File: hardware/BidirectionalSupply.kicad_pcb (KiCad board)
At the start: 4 copper layers, 132 x 107 mm, 182 parts, among them J1 USB-309GC-B-SU, J10 Conn_01x02, J11 Conn_01x08, J12 Conn_01x05, J13 Conn_01x02, J2 CON10, J3 CON2, J6 CON4, J7 CON2, J8 Conn_01x03, J9 Conn_01x12, Q1 SIR880BDP, Q10 SIR880BDP, Q11 SIR880BDP, Q12 SIR880BDP, Q2 SIR880BDP, Q3 SIR880BDP, Q4 SIR880BDP, Q5 SIR880BDP, Q6 SIR880BDP, Q7 SIR880BDP, Q8 SIR880BDP, Q9 SIR880BDP, SW1 SW_Push, SW2 SW_Push, U1 W25Q128JVS, U2 LM74810QDRRRQ1, U3 RP2350_60QFN, U4 BQ25758, U5 MAX17502EATB+T, U6 LM74810QDRRRQ1, U7 LM74810QDRRRQ1, U8 LM74810QDRRRQ1, Y1 ABM8-272-T3

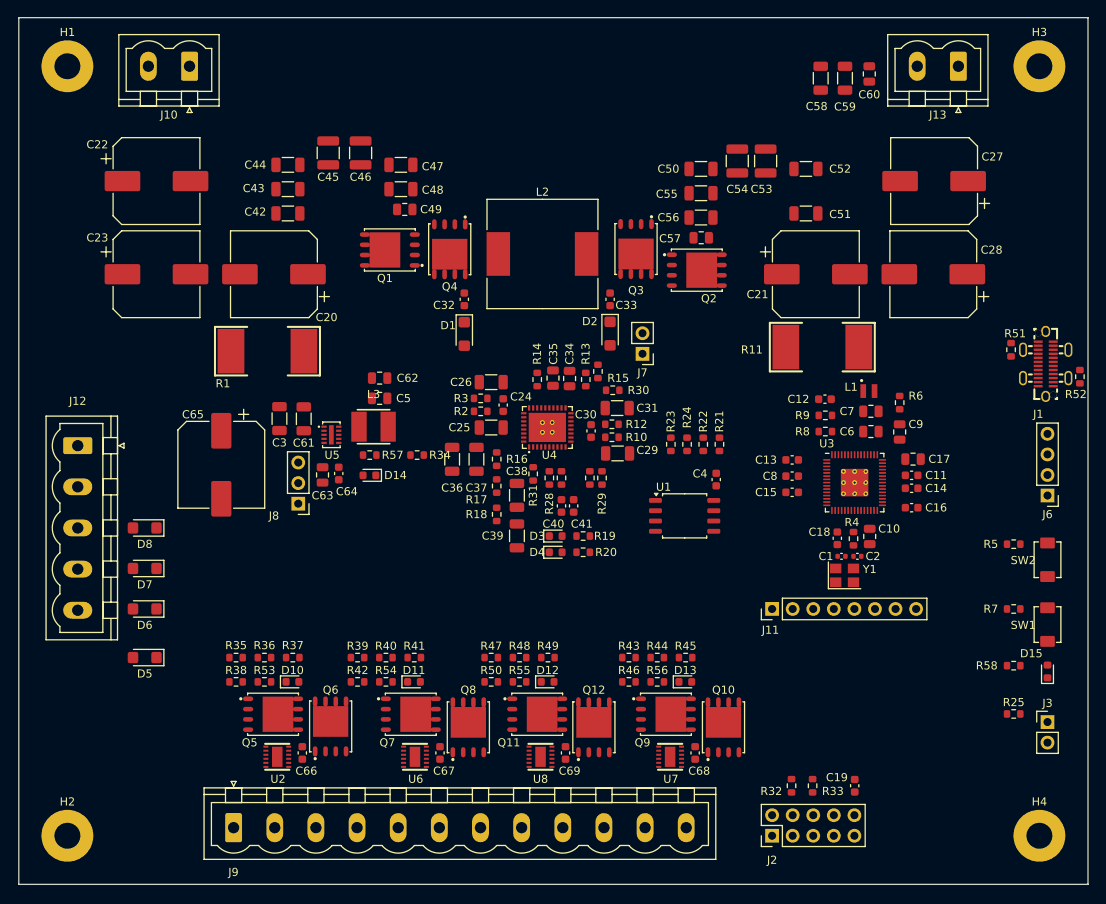
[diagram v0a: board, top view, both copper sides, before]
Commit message: - Routed board with all fixable DRC errors and warnings fixed
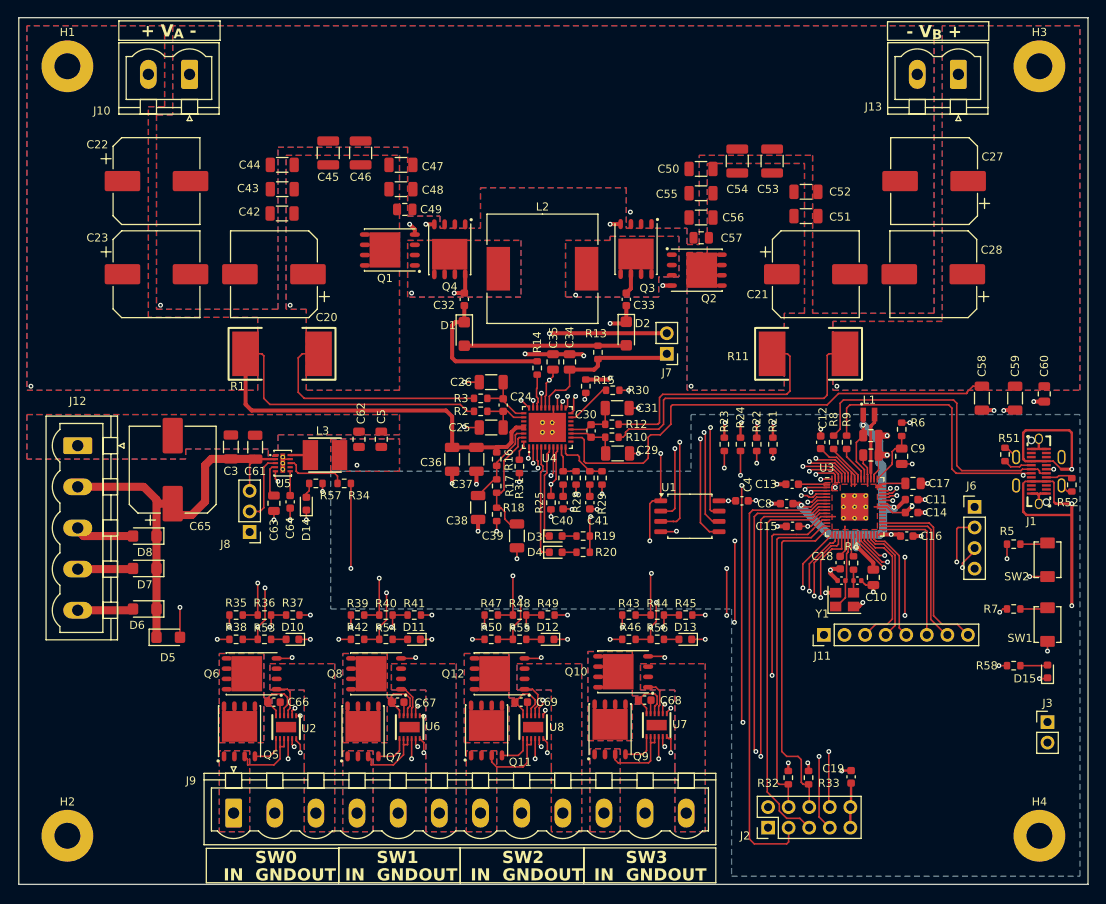
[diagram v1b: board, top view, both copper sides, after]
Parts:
- C1, C2: footprint Capacitor_SMD:C_0402_1005Metric -> BidirectionalSupply:C_0402_DRC
- Y1: footprint Crystal:Crystal_SMD_3225-4Pin_3.2x2.5mm -> BidirectionalSupply:Crystal_SMD_3225-4Pin_DRC
- moved R25 62.8 mm to (115.7, 109.9), turned to 90 degrees
- moved C60 45.0 mm to (176.6, 96.5)
- moved C59 44.7 mm to (173.0, 97.0)
- moved C58 44.2 mm to (168.9, 97.0)
- moved Q10 14.2 mm to (124.6, 130.8), turned to 90 degrees
- moved R52 13.4 mm to (180.0, 107.7)
- moved Q12 13.4 mm to (109.4, 131.0), turned to 90 degrees
- moved J1 13.3 mm to (175.9, 106.0)
- moved Q8 13.2 mm to (94.1, 131.0), turned to 90 degrees
- moved R51 12.9 mm to (171.8, 103.9)
- moved Q6 11.7 mm to (78.8, 131.0), turned to 90 degrees
- moved R34 9.66 mm to (90.2, 107.5)
- moved J6 9.11 mm to (168.0, 110.4), turned to 0 degrees
- moved C68 9.02 mm to (127.3, 134.2), turned to 0 degrees
- moved D14 8.54 mm to (85.5, 110.0), turned to 90 degrees
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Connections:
- C27 pad 1: Net-(J13-Pin_2) -> Net-(J13-Pin_1)
- C28 pad 1: Net-(J13-Pin_2) -> Net-(J13-Pin_1)
- C58 pad 1: Net-(J13-Pin_2) -> Net-(J13-Pin_1)
- C59 pad 1: Net-(J13-Pin_2) -> Net-(J13-Pin_1)
- C60 pad 1: Net-(J13-Pin_2) -> Net-(J13-Pin_1)
- J11 pad 1: Net-(J11-Pin_1) -> GND
- J11 pad 2: Net-(J11-Pin_2) -> +3V3
- J13 pad 1: GND -> Net-(J13-Pin_1)
- J13 pad 2: Net-(J13-Pin_2) -> GND
- J9 pad 1: GND -> Net-(J9-Pin_1)
- J9 pad 10: GND -> Net-(J9-Pin_10)
- J9 pad 11: Net-(J9-Pin_11) -> GND
- J9 pad 2: Net-(J9-Pin_2) -> GND
- J9 pad 4: GND -> Net-(J9-Pin_4)
- J9 pad 5: Net-(J9-Pin_5) -> GND
- J9 pad 7: GND -> Net-(J9-Pin_7)
- J9 pad 8: Net-(J9-Pin_8) -> GND
- Q11 pad 1: Net-(J9-Pin_8) -> Net-(J9-Pin_7)
- Q11 pad 2: Net-(J9-Pin_8) -> Net-(J9-Pin_7)
- Q11 pad 3: Net-(J9-Pin_8) -> Net-(J9-Pin_7)
- Q5 pad 1: Net-(J9-Pin_2) -> Net-(J9-Pin_1)
- Q5 pad 2: Net-(J9-Pin_2) -> Net-(J9-Pin_1)
- Q5 pad 3: Net-(J9-Pin_2) -> Net-(J9-Pin_1)
- Q7 pad 1: Net-(J9-Pin_5) -> Net-(J9-Pin_4)
- Q7 pad 2: Net-(J9-Pin_5) -> Net-(J9-Pin_4)
- Q7 pad 3: Net-(J9-Pin_5) -> Net-(J9-Pin_4)
- Q9 pad 1: Net-(J9-Pin_11) -> Net-(J9-Pin_10)
- Q9 pad 2: Net-(J9-Pin_11) -> Net-(J9-Pin_10)
- Q9 pad 3: Net-(J9-Pin_11) -> Net-(J9-Pin_10)
- R10 pad 1: Net-(J13-Pin_2) -> Net-(J13-Pin_1)
- R11 pad 1: Net-(J13-Pin_2) -> Net-(J13-Pin_1)
- U2 pad 2: Net-(J9-Pin_2) -> Net-(J9-Pin_1)
- U2 pad 3: Net-(J9-Pin_2) -> Net-(J9-Pin_1)
- U3 pad 16: Net-(J11-Pin_1) -> SW0_EN
- U3 pad 17: Net-(J11-Pin_2) -> SW1_EN
- U3 pad 18: Net-(J11-Pin_3) -> SW2_EN
- U3 pad 19: Net-(J11-Pin_4) -> SW3_EN
- U3 pad 27: Net-(J11-Pin_5) -> Net-(J11-Pin_3)
- U3 pad 28: Net-(J11-Pin_6) -> Net-(J11-Pin_4)
- U3 pad 29: Net-(J11-Pin_7) -> Net-(J11-Pin_5)
- U3 pad 31: Net-(J11-Pin_8) -> Net-(J11-Pin_6)
- U3 pad 32: unconnected-(U3-GPIO20-Pad32) -> Net-(J11-Pin_7)
- U3 pad 33: unconnected-(U3-GPIO21-Pad33) -> Net-(J11-Pin_8)
- U3 pad 34: SW0_EN -> unconnected-(U3-GPIO22-Pad34)
- U3 pad 35: SW1_EN -> unconnected-(U3-GPIO23-Pad35)
- U3 pad 36: SW2_EN -> unconnected-(U3-GPIO24-Pad36)
- U3 pad 37: SW3_EN -> unconnected-(U3-GPIO25-Pad37)
- U3 pad 4: ~{BQ_CE} -> ~{BQ_INT}
- U3 pad 5: ~{BQ_INT} -> ~{BQ_CE}
- U4 pad 12: Net-(J13-Pin_2) -> Net-(J13-Pin_1)
- U6 pad 2: Net-(J9-Pin_5) -> Net-(J9-Pin_4)
- U6 pad 3: Net-(J9-Pin_5) -> Net-(J9-Pin_4)
- U7 pad 2: Net-(J9-Pin_11) -> Net-(J9-Pin_10)
- U7 pad 3: Net-(J9-Pin_11) -> Net-(J9-Pin_10)
- U8 pad 2: Net-(J9-Pin_8) -> Net-(J9-Pin_7)
- U8 pad 3: Net-(J9-Pin_8) -> Net-(J9-Pin_7)
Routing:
- net Net-(D5-A): track 0.00 -> 169.6 mm, vias 0 -> 4
- net Net-(U3-RUN): track 0.00 -> 113.0 mm, vias 0 -> 7
- net SW0_EN: track 0.00 -> 105.4 mm, vias 0 -> 4
- net GND: track 0.00 -> 102.1 mm, vias 0 -> 61
- net Net-(J13-Pin_1): track 0.00 -> 97.5 mm, vias 0 -> 1
- net Net-(J3-Pin_1): track 0.00 -> 96.9 mm, vias 0 -> 3
- net SW0_VSENSE: track 0.00 -> 94.4 mm, vias 0 -> 2
- net SW1_EN: track 0.00 -> 91.6 mm, vias 0 -> 4
- net /Microcontroller/QSPI_SS: track 0.00 -> 90.9 mm, vias 0 -> 6
- net CNV_VIN: track 0.00 -> 82.5 mm, vias 0 -> 1
- net SW1_VSENSE: track 0.00 -> 81.4 mm, vias 0 -> 2
- net SW2_EN: track 0.00 -> 74.5 mm, vias 0 -> 4
- net +3V3: track 0.00 -> 72.8 mm, vias 0 -> 16
- net SW2_VSENSE: track 0.00 -> 65.7 mm, vias 0 -> 2
- net LED: track 0.00 -> 59.0 mm, vias 0 -> 2
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- added copper zone on B.Cu, net +3V3
- added copper zone on F.Cu, net +3V3
- added copper zone on B.Cu, net CNV_VIN
- added copper zone on F.Cu, net CNV_VIN
- added copper zone on B.Cu, net GND
- added copper zone on F.Cu, net GND
- added copper zone on In1.Cu, net GND
- added copper zone on B.Cu, net Net-(J13-Pin_1)
- added copper zone on F.Cu, net Net-(J13-Pin_1)
- added copper zone on B.Cu, net Net-(J9-Pin_1)
- added copper zone on F.Cu, net Net-(J9-Pin_1)
- added copper zone on B.Cu, net Net-(J9-Pin_10)
- added copper zone on F.Cu, net Net-(J9-Pin_10)
- added copper zone on B.Cu, net Net-(J9-Pin_12)
- added copper zone on F.Cu, net Net-(J9-Pin_12)
- added copper zone on B.Cu, net Net-(J9-Pin_3)
- added copper zone on F.Cu, net Net-(J9-Pin_3)
- added copper zone on B.Cu, net Net-(J9-Pin_4)
- added copper zone on F.Cu, net Net-(J9-Pin_4)
- added copper zone on B.Cu, net Net-(J9-Pin_6)
- added copper zone on F.Cu, net Net-(J9-Pin_6)
- added copper zone on B.Cu, net Net-(J9-Pin_7)
- added copper zone on F.Cu, net Net-(J9-Pin_7)
- added copper zone on B.Cu, net Net-(J9-Pin_9)
- added copper zone on F.Cu, net Net-(J9-Pin_9)
- added copper zone on B.Cu, net Net-(Q1-EP)
- added copper zone on F.Cu, net Net-(Q1-EP)
- added copper zone on B.Cu, net Net-(Q10-EP)
- added copper zone on F.Cu, net Net-(Q10-EP)
- added copper zone on B.Cu, net Net-(Q11-EP)
- added copper zone on F.Cu, net Net-(Q11-EP)
- added copper zone on B.Cu, net Net-(Q2-EP)
- added copper zone on F.Cu, net Net-(Q2-EP)
- added copper zone on B.Cu, net Net-(Q3-EP)
- added copper zone on F.Cu, net Net-(Q3-EP)
- added copper zone on B.Cu, net Net-(Q4-EP)
- added copper zone on F.Cu, net Net-(Q4-EP)
- added copper zone on B.Cu, net Net-(Q5-EP)
- added copper zone on F.Cu, net Net-(Q5-EP)
- added copper zone on B.Cu, net Net-(Q7-EP)
- added copper zone on F.Cu, net Net-(Q7-EP)
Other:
- board text added: "+ V_{A} -"
- board text added: "- V_{B} +"
- board text added: "GND"
- board text added: "IN"
- board text added: "OUT"
- board text added: "SW0"
- board text added: "SW1"
- board text added: "SW2"
- board text added: "SW3"

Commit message: Added summary page Added prototyping area to PCB
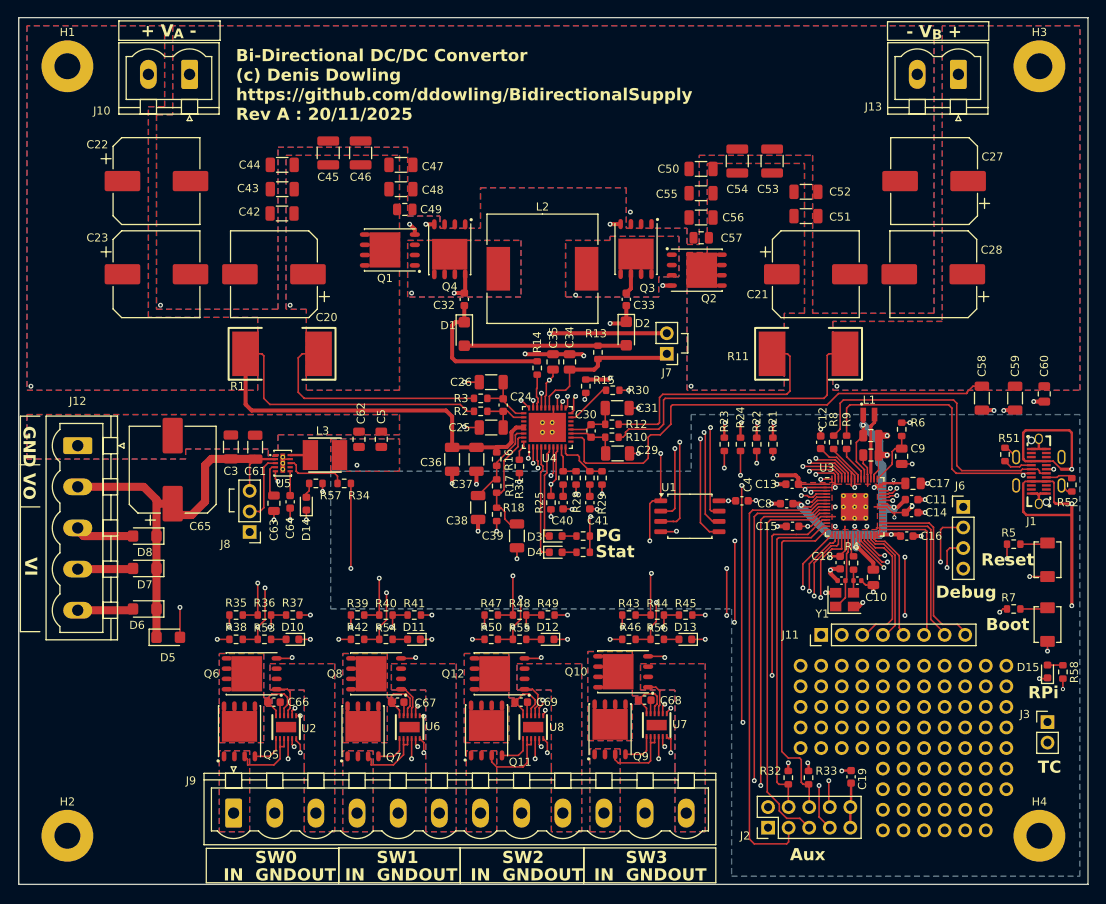
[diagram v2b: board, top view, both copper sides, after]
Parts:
- added ?: , , F.Cu at (169.4, 137.6)
- added ?: , , F.Cu at (171.9, 135.1)
- added ?: , , F.Cu at (169.4, 140.2)
- added ?: , , F.Cu at (171.9, 132.6)
- added ?: , , F.Cu at (169.4, 135.1)
- added ?: , , F.Cu at (171.9, 140.2)
- added ?: , , F.Cu at (169.4, 132.6)
- added ?: , , F.Cu at (171.9, 130.0)
- added ?: , , F.Cu at (171.9, 137.6)
- added REF**: Pad_D1.7mm_Drill1.0mm, BidirectionalSupply:Pad_D1.7mm_Drill1.0mm, F.Cu at (151.6, 132.6)
- added REF**: Pad_D1.7mm_Drill1.0mm, BidirectionalSupply:Pad_D1.7mm_Drill1.0mm, F.Cu at (159.2, 150.3)
- added REF**: Pad_D1.7mm_Drill1.0mm, BidirectionalSupply:Pad_D1.7mm_Drill1.0mm, F.Cu at (156.7, 140.2)
- added REF**: Pad_D1.7mm_Drill1.0mm, BidirectionalSupply:Pad_D1.7mm_Drill1.0mm, F.Cu at (156.7, 132.6)
- added REF**: Pad_D1.7mm_Drill1.0mm, BidirectionalSupply:Pad_D1.7mm_Drill1.0mm, F.Cu at (166.8, 147.8)
- added REF**: Pad_D1.7mm_Drill1.0mm, BidirectionalSupply:Pad_D1.7mm_Drill1.0mm, F.Cu at (154.1, 135.1)
- added REF**: Pad_D1.7mm_Drill1.0mm, BidirectionalSupply:Pad_D1.7mm_Drill1.0mm, F.Cu at (164.3, 150.3)
- added REF**: Pad_D1.7mm_Drill1.0mm, BidirectionalSupply:Pad_D1.7mm_Drill1.0mm, F.Cu at (146.5, 137.6)
- added REF**: Pad_D1.7mm_Drill1.0mm, BidirectionalSupply:Pad_D1.7mm_Drill1.0mm, F.Cu at (146.5, 132.6)
- added REF**: Pad_D1.7mm_Drill1.0mm, BidirectionalSupply:Pad_D1.7mm_Drill1.0mm, F.Cu at (159.2, 142.7)
- added REF**: Pad_D1.7mm_Drill1.0mm, BidirectionalSupply:Pad_D1.7mm_Drill1.0mm, F.Cu at (161.8, 137.6)
- added REF**: Pad_D1.7mm_Drill1.0mm, BidirectionalSupply:Pad_D1.7mm_Drill1.0mm, F.Cu at (156.7, 135.1)
- added REF**: Pad_D1.7mm_Drill1.0mm, BidirectionalSupply:Pad_D1.7mm_Drill1.0mm, F.Cu at (146.5, 135.1)
- added REF**: Pad_D1.7mm_Drill1.0mm, BidirectionalSupply:Pad_D1.7mm_Drill1.0mm, F.Cu at (164.3, 135.1)
- added REF**: Pad_D1.7mm_Drill1.0mm, BidirectionalSupply:Pad_D1.7mm_Drill1.0mm, F.Cu at (169.4, 150.3)
- added REF**: Pad_D1.7mm_Drill1.0mm, BidirectionalSupply:Pad_D1.7mm_Drill1.0mm, F.Cu at (149.1, 132.6)
- added REF**: Pad_D1.7mm_Drill1.0mm, BidirectionalSupply:Pad_D1.7mm_Drill1.0mm, F.Cu at (159.2, 135.1)
- added REF**: Pad_D1.7mm_Drill1.0mm, BidirectionalSupply:Pad_D1.7mm_Drill1.0mm, F.Cu at (161.8, 132.6)
- added REF**: Pad_D1.7mm_Drill1.0mm, BidirectionalSupply:Pad_D1.7mm_Drill1.0mm, F.Cu at (164.3, 140.2)
- added REF**: Pad_D1.7mm_Drill1.0mm, BidirectionalSupply:Pad_D1.7mm_Drill1.0mm, F.Cu at (159.2, 145.2)
- added REF**: Pad_D1.7mm_Drill1.0mm, BidirectionalSupply:Pad_D1.7mm_Drill1.0mm, F.Cu at (166.8, 145.2)
- added REF**: Pad_D1.7mm_Drill1.0mm, BidirectionalSupply:Pad_D1.7mm_Drill1.0mm, F.Cu at (156.7, 147.8)
- added REF**: Pad_D1.7mm_Drill1.0mm, BidirectionalSupply:Pad_D1.7mm_Drill1.0mm, F.Cu at (149.1, 135.1)
- added REF**: Pad_D1.7mm_Drill1.0mm, BidirectionalSupply:Pad_D1.7mm_Drill1.0mm, F.Cu at (169.4, 142.7)
- added REF**: Pad_D1.7mm_Drill1.0mm, BidirectionalSupply:Pad_D1.7mm_Drill1.0mm, F.Cu at (161.8, 135.1)
- added REF**: Pad_D1.7mm_Drill1.0mm, BidirectionalSupply:Pad_D1.7mm_Drill1.0mm, F.Cu at (156.7, 150.3)
- added REF**: Pad_D1.7mm_Drill1.0mm, BidirectionalSupply:Pad_D1.7mm_Drill1.0mm, F.Cu at (156.7, 137.6)
- added REF**: Pad_D1.7mm_Drill1.0mm, BidirectionalSupply:Pad_D1.7mm_Drill1.0mm, F.Cu at (151.6, 130.0)
- added REF**: Pad_D1.7mm_Drill1.0mm, BidirectionalSupply:Pad_D1.7mm_Drill1.0mm, F.Cu at (164.3, 147.8)
- added REF**: Pad_D1.7mm_Drill1.0mm, BidirectionalSupply:Pad_D1.7mm_Drill1.0mm, F.Cu at (154.1, 130.0)
- added REF**: Pad_D1.7mm_Drill1.0mm, BidirectionalSupply:Pad_D1.7mm_Drill1.0mm, F.Cu at (166.8, 150.3)
- added REF**: Pad_D1.7mm_Drill1.0mm, BidirectionalSupply:Pad_D1.7mm_Drill1.0mm, F.Cu at (164.3, 130.0)
- added REF**: Pad_D1.7mm_Drill1.0mm, BidirectionalSupply:Pad_D1.7mm_Drill1.0mm, F.Cu at (151.6, 140.2)
- added REF**: Pad_D1.7mm_Drill1.0mm, BidirectionalSupply:Pad_D1.7mm_Drill1.0mm, F.Cu at (161.8, 140.2)
- added REF**: Pad_D1.7mm_Drill1.0mm, BidirectionalSupply:Pad_D1.7mm_Drill1.0mm, F.Cu at (154.1, 140.2)
- added REF**: Pad_D1.7mm_Drill1.0mm, BidirectionalSupply:Pad_D1.7mm_Drill1.0mm, F.Cu at (159.2, 130.0)
- added REF**: Pad_D1.7mm_Drill1.0mm, BidirectionalSupply:Pad_D1.7mm_Drill1.0mm, F.Cu at (154.1, 137.6)
- added REF**: Pad_D1.7mm_Drill1.0mm, BidirectionalSupply:Pad_D1.7mm_Drill1.0mm, F.Cu at (159.2, 147.8)
- added REF**: Pad_D1.7mm_Drill1.0mm, BidirectionalSupply:Pad_D1.7mm_Drill1.0mm, F.Cu at (159.2, 132.6)
- added REF**: Pad_D1.7mm_Drill1.0mm, BidirectionalSupply:Pad_D1.7mm_Drill1.0mm, F.Cu at (164.3, 132.6)
- added REF**: Pad_D1.7mm_Drill1.0mm, BidirectionalSupply:Pad_D1.7mm_Drill1.0mm, F.Cu at (154.1, 132.6)
- added REF**: Pad_D1.7mm_Drill1.0mm, BidirectionalSupply:Pad_D1.7mm_Drill1.0mm, F.Cu at (159.2, 140.2)
- added REF**: Pad_D1.7mm_Drill1.0mm, BidirectionalSupply:Pad_D1.7mm_Drill1.0mm, F.Cu at (161.8, 145.2)
- added REF**: Pad_D1.7mm_Drill1.0mm, BidirectionalSupply:Pad_D1.7mm_Drill1.0mm, F.Cu at (166.8, 142.7)
- added REF**: Pad_D1.7mm_Drill1.0mm, BidirectionalSupply:Pad_D1.7mm_Drill1.0mm, F.Cu at (166.8, 135.1)
- added REF**: Pad_D1.7mm_Drill1.0mm, BidirectionalSupply:Pad_D1.7mm_Drill1.0mm, F.Cu at (149.1, 140.2)
- added REF**: Pad_D1.7mm_Drill1.0mm, BidirectionalSupply:Pad_D1.7mm_Drill1.0mm, F.Cu at (164.3, 142.7)
- added REF**: Pad_D1.7mm_Drill1.0mm, BidirectionalSupply:Pad_D1.7mm_Drill1.0mm, F.Cu at (166.8, 130.0)
- added REF**: Pad_D1.7mm_Drill1.0mm, BidirectionalSupply:Pad_D1.7mm_Drill1.0mm, F.Cu at (161.8, 142.7)
- added REF**: Pad_D1.7mm_Drill1.0mm, BidirectionalSupply:Pad_D1.7mm_Drill1.0mm, F.Cu at (169.4, 145.2)
- added REF**: Pad_D1.7mm_Drill1.0mm, BidirectionalSupply:Pad_D1.7mm_Drill1.0mm, F.Cu at (156.7, 142.7)
- added REF**: Pad_D1.7mm_Drill1.0mm, BidirectionalSupply:Pad_D1.7mm_Drill1.0mm, F.Cu at (166.8, 137.6)
- added REF**: Pad_D1.7mm_Drill1.0mm, BidirectionalSupply:Pad_D1.7mm_Drill1.0mm, F.Cu at (151.6, 137.6)
- added REF**: Pad_D1.7mm_Drill1.0mm, BidirectionalSupply:Pad_D1.7mm_Drill1.0mm, F.Cu at (171.9, 145.2)
- added REF**: Pad_D1.7mm_Drill1.0mm, BidirectionalSupply:Pad_D1.7mm_Drill1.0mm, F.Cu at (164.3, 145.2)
- added REF**: Pad_D1.7mm_Drill1.0mm, BidirectionalSupply:Pad_D1.7mm_Drill1.0mm, F.Cu at (169.4, 130.0)
- added REF**: Pad_D1.7mm_Drill1.0mm, BidirectionalSupply:Pad_D1.7mm_Drill1.0mm, F.Cu at (166.8, 132.6)
- added REF**: Pad_D1.7mm_Drill1.0mm, BidirectionalSupply:Pad_D1.7mm_Drill1.0mm, F.Cu at (159.2, 137.6)
- added REF**: Pad_D1.7mm_Drill1.0mm, BidirectionalSupply:Pad_D1.7mm_Drill1.0mm, F.Cu at (149.1, 137.6)
- added REF**: Pad_D1.7mm_Drill1.0mm, BidirectionalSupply:Pad_D1.7mm_Drill1.0mm, F.Cu at (151.6, 135.1)
- added REF**: Pad_D1.7mm_Drill1.0mm, BidirectionalSupply:Pad_D1.7mm_Drill1.0mm, F.Cu at (166.8, 140.2)
- added REF**: Pad_D1.7mm_Drill1.0mm, BidirectionalSupply:Pad_D1.7mm_Drill1.0mm, F.Cu at (156.7, 130.0)
- added REF**: Pad_D1.7mm_Drill1.0mm, BidirectionalSupply:Pad_D1.7mm_Drill1.0mm, F.Cu at (156.7, 145.2)
- added REF**: Pad_D1.7mm_Drill1.0mm, BidirectionalSupply:Pad_D1.7mm_Drill1.0mm, F.Cu at (146.5, 130.0)
- added REF**: Pad_D1.7mm_Drill1.0mm, BidirectionalSupply:Pad_D1.7mm_Drill1.0mm, F.Cu at (149.1, 130.0)
- added REF**: Pad_D1.7mm_Drill1.0mm, BidirectionalSupply:Pad_D1.7mm_Drill1.0mm, F.Cu at (169.4, 147.8)
- added REF**: Pad_D1.7mm_Drill1.0mm, BidirectionalSupply:Pad_D1.7mm_Drill1.0mm, F.Cu at (171.9, 142.7)
- added REF**: Pad_D1.7mm_Drill1.0mm, BidirectionalSupply:Pad_D1.7mm_Drill1.0mm, F.Cu at (161.8, 150.3)
- added REF**: Pad_D1.7mm_Drill1.0mm, BidirectionalSupply:Pad_D1.7mm_Drill1.0mm, F.Cu at (161.8, 147.8)
- added REF**: Pad_D1.7mm_Drill1.0mm, BidirectionalSupply:Pad_D1.7mm_Drill1.0mm, F.Cu at (164.3, 137.6)
- added REF**: Pad_D1.7mm_Drill1.0mm, BidirectionalSupply:Pad_D1.7mm_Drill1.0mm, F.Cu at (161.8, 130.0)
- added REF**: Pad_D1.7mm_Drill1.0mm, BidirectionalSupply:Pad_D1.7mm_Drill1.0mm, F.Cu at (146.5, 140.2)
- moved R58 6.12 mm to (178.9, 130.8), turned to 90 degrees
- moved J6 1.40 mm to (166.6, 110.4)
- moved J11 0.34 mm to (149.1, 126.2)
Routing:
- net +3V3: track 72.8 -> 79.1 mm, vias 16 -> 26
- net Net-(J6-Pin_2): track 20.1 -> 18.7 mm
- net Net-(D15-A): track 3.38 -> 2.02 mm
- net Net-(J6-Pin_3): track 18.1 -> 17.4 mm
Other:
- board text added: "Aux"
- board text added: "Bi-Directional DC/DC Convertor (c) Denis Dowling https://github.com/ddowling/BidirectionalSupply Rev A : 20/11/2025"
- board text added: "Boot"
- board text added: "Debug"
- board text added: "PG"
- board text added: "RPi"
- board text added: "Reset"
- board text added: "Stat"
- board text added: "TC"
- board text added: "VI"
- board text added: "VO"

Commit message: Ready for trial submit to JLCPCB
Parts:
- removed ? (x9): , 
- removed REF** (x72): Pad_D1.7mm_Drill1.0mm, BidirectionalSupply:Pad_D1.7mm_Drill1.0mm
- added C70: 100nF/100VW, Capacitor_SMD:C_1206_3216Metric, F.Cu at (71.9, 129.1)
- added C71: 100nF/100VW, Capacitor_SMD:C_1206_3216Metric, F.Cu at (87.4, 128.8)
- added C72: 100nF/100VW, Capacitor_SMD:C_1206_3216Metric, F.Cu at (102.7, 128.6)
- added C73: 100nF/100VW, Capacitor_SMD:C_1206_3216Metric, F.Cu at (118.0, 128.8)
- added R59: 0R, Resistor_SMD:R_0603_1608Metric, F.Cu at (74.3, 124.6)
- added R60: 0R, Resistor_SMD:R_0603_1608Metric, F.Cu at (89.3, 124.6)
- added R61: 0R, Resistor_SMD:R_0603_1608Metric, F.Cu at (122.8, 124.6)
- added R62: 0R, Resistor_SMD:R_0603_1608Metric, F.Cu at (105.7, 124.6)
- moved J9 55.5 mm to (132.0, 147.0), turned to 180 degrees
- moved J12 20.3 mm to (58.5, 123.1), turned to 90 degrees
- moved J10 5.30 mm to (66.0, 58.5), turned to 0 degrees
- moved J13 5.22 mm to (161.0, 58.5), turned to 0 degrees
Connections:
- C27 pad 1: Net-(J13-Pin_1) -> Net-(J13-Pin_2)
- C28 pad 1: Net-(J13-Pin_1) -> Net-(J13-Pin_2)
- C58 pad 1: Net-(J13-Pin_1) -> Net-(J13-Pin_2)
- C59 pad 1: Net-(J13-Pin_1) -> Net-(J13-Pin_2)
- C60 pad 1: Net-(J13-Pin_1) -> Net-(J13-Pin_2)
- J10 pad 1: GND -> CNV_VIN
- J10 pad 2: CNV_VIN -> GND
- J12 pad 1: GND -> Net-(D6-A)
- J12 pad 2: Net-(D5-K) -> Net-(D7-A)
- J12 pad 4: Net-(D7-A) -> Net-(D5-K)
- J12 pad 5: Net-(D6-A) -> GND
- J13 pad 1: Net-(J13-Pin_1) -> GND
- J13 pad 2: GND -> Net-(J13-Pin_2)
- Q10 pad 1: Net-(J9-Pin_12) -> Net-(J9-Pin_1)
- Q10 pad 2: Net-(J9-Pin_12) -> Net-(J9-Pin_1)
- Q10 pad 3: Net-(J9-Pin_12) -> Net-(J9-Pin_1)
- Q11 pad 1: Net-(J9-Pin_7) -> Net-(J9-Pin_6)
- Q11 pad 2: Net-(J9-Pin_7) -> Net-(J9-Pin_6)
- Q11 pad 3: Net-(J9-Pin_7) -> Net-(J9-Pin_6)
- Q12 pad 1: Net-(J9-Pin_9) -> Net-(J9-Pin_4)
- Q12 pad 2: Net-(J9-Pin_9) -> Net-(J9-Pin_4)
- Q12 pad 3: Net-(J9-Pin_9) -> Net-(J9-Pin_4)
- Q5 pad 1: Net-(J9-Pin_1) -> Net-(J9-Pin_12)
- Q5 pad 2: Net-(J9-Pin_1) -> Net-(J9-Pin_12)
- Q5 pad 3: Net-(J9-Pin_1) -> Net-(J9-Pin_12)
- Q6 pad 1: Net-(J9-Pin_3) -> Net-(J9-Pin_10)
- Q6 pad 2: Net-(J9-Pin_3) -> Net-(J9-Pin_10)
- Q6 pad 3: Net-(J9-Pin_3) -> Net-(J9-Pin_10)
- Q7 pad 1: Net-(J9-Pin_4) -> Net-(J9-Pin_9)
- Q7 pad 2: Net-(J9-Pin_4) -> Net-(J9-Pin_9)
- Q7 pad 3: Net-(J9-Pin_4) -> Net-(J9-Pin_9)
- Q8 pad 1: Net-(J9-Pin_6) -> Net-(J9-Pin_7)
- Q8 pad 2: Net-(J9-Pin_6) -> Net-(J9-Pin_7)
- Q8 pad 3: Net-(J9-Pin_6) -> Net-(J9-Pin_7)
- Q9 pad 1: Net-(J9-Pin_10) -> Net-(J9-Pin_3)
- Q9 pad 2: Net-(J9-Pin_10) -> Net-(J9-Pin_3)
- Q9 pad 3: Net-(J9-Pin_10) -> Net-(J9-Pin_3)
- R10 pad 1: Net-(J13-Pin_1) -> Net-(J13-Pin_2)
- R11 pad 1: Net-(J13-Pin_1) -> Net-(J13-Pin_2)
- U2 pad 2: Net-(J9-Pin_1) -> Net-(J9-Pin_12)
- U2 pad 3: Net-(J9-Pin_1) -> Net-(J9-Pin_12)
- U2 pad 9: Net-(J9-Pin_3) -> Net-(J9-Pin_10)
- U4 pad 12: Net-(J13-Pin_1) -> Net-(J13-Pin_2)
- U6 pad 2: Net-(J9-Pin_4) -> Net-(J9-Pin_9)
- U6 pad 3: Net-(J9-Pin_4) -> Net-(J9-Pin_9)
- U6 pad 9: Net-(J9-Pin_6) -> Net-(J9-Pin_7)
- U7 pad 2: Net-(J9-Pin_10) -> Net-(J9-Pin_3)
- U7 pad 3: Net-(J9-Pin_10) -> Net-(J9-Pin_3)
- U7 pad 9: Net-(J9-Pin_12) -> Net-(J9-Pin_1)
- U8 pad 2: Net-(J9-Pin_7) -> Net-(J9-Pin_6)
- U8 pad 3: Net-(J9-Pin_7) -> Net-(J9-Pin_6)
- U8 pad 9: Net-(J9-Pin_9) -> Net-(J9-Pin_4)
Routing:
- net Net-(J13-Pin_1): track 97.5 -> 0.00 mm, vias 1 -> 0
- net Net-(J13-Pin_2): track 0.00 -> 80.1 mm, vias 0 -> 48
- net Net-(J9-Pin_12): track 4.49 -> 29.4 mm, vias 0 -> 2
- net Net-(J9-Pin_3): track 4.84 -> 29.3 mm, vias 0 -> 2
- net Net-(J9-Pin_6): track 4.19 -> 28.4 mm, vias 0 -> 2
- net Net-(J9-Pin_9): track 4.65 -> 28.5 mm, vias 0 -> 2
- net CNV_VIN: track 82.5 -> 97.8 mm, vias 1 -> 54
- net GND: track 102.1 -> 108.6 mm, vias 61 -> 276
- net Net-(J9-Pin_7): track 9.88 -> 4.19 mm, vias 0 -> 7
- net Net-(J9-Pin_1): track 9.52 -> 4.49 mm, vias 0 -> 6
- net Net-(J9-Pin_10): track 9.57 -> 4.84 mm, vias 0 -> 5
- net AUX_SPI_RX: track 57.2 -> 52.6 mm
- net Net-(J9-Pin_4): track 8.98 -> 4.65 mm, vias 0 -> 6
- net Net-(Q11-EP): track 7.47 -> 9.76 mm, vias 0 -> 16
- net Net-(Q5-EP): track 7.86 -> 10.1 mm, vias 0 -> 17
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- added copper zone on In2.Cu, net GND
- added copper zone on B.Cu, net Net-(J13-Pin_2)
- added copper zone on F.Cu, net Net-(J13-Pin_2)
- removed copper zone on B.Cu, net Net-(J13-Pin_1)
- removed copper zone on F.Cu, net Net-(J13-Pin_1)
